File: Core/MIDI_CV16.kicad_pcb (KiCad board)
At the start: 2 copper layers, 59.5 x 99.5 mm, 166 parts, among them J1 USB_C_Receptacle_USB2.0, J2 Conn_01x06_Male, J20 Conn_02x08_Odd_Even, J3 Conn_01x10_Female, J4 Conn_01x10_Female, J5 Conn_01x04, J7 Conn_01x10_Female, J8 Conn_01x10_Female, Q1 BSS84, Q10 BSS84, Q11 2N7002, Q12 2N7002, Q13 BSS84, Q14 2N7002, Q15 BSS84, Q16 BSS84, Q17 2N7002, Q2 BSS84, Q3 2N7002, Q4 BSS84, Q5 BSS84, Q6 2N7002, Q7 BSS84, Q8 2N7002, Q9 BSS84, SW1 SW_Push_DPDT, SW2 SW_SPST, SW3 SW_SPST, U1 RP2040, U10 TL072, U11 TL072, U12 TL072, U13 MCP2517FD-xSL, U14 TLE9250V, U15 MAX5134, U16 CAT25640, U17 IS25LP032D, U2 TMUX4052, U3 MIC5504-3.3YM5, U4 TL072, U5 TL072, U6 TL072, U7 TL072, U8 TMUX4052, U9 TL072, Y1 20MHz, Y2 ECS-120-18-33-JGN-TR3

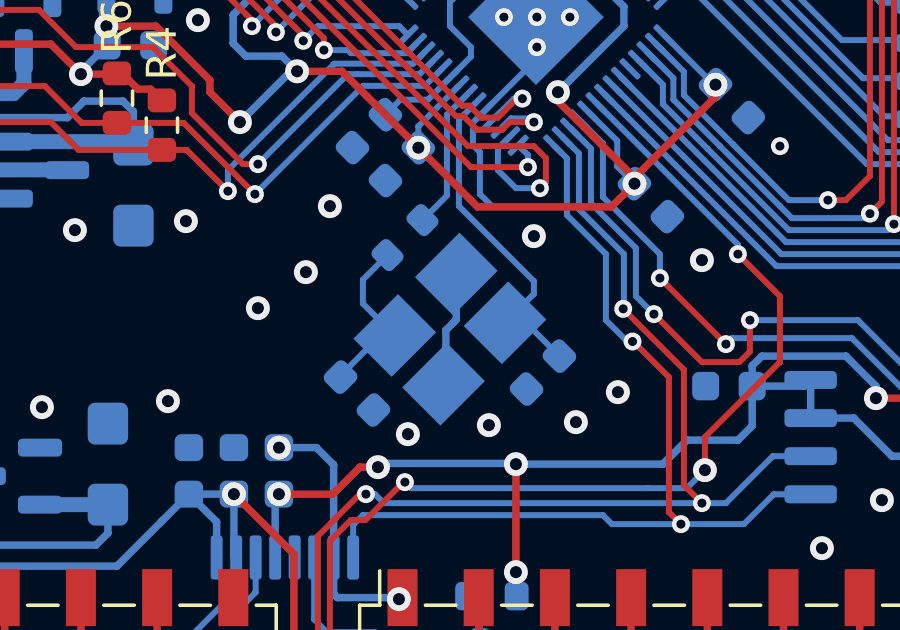
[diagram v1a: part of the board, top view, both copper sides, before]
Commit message: Shrink crystal fp and add silkscreen text
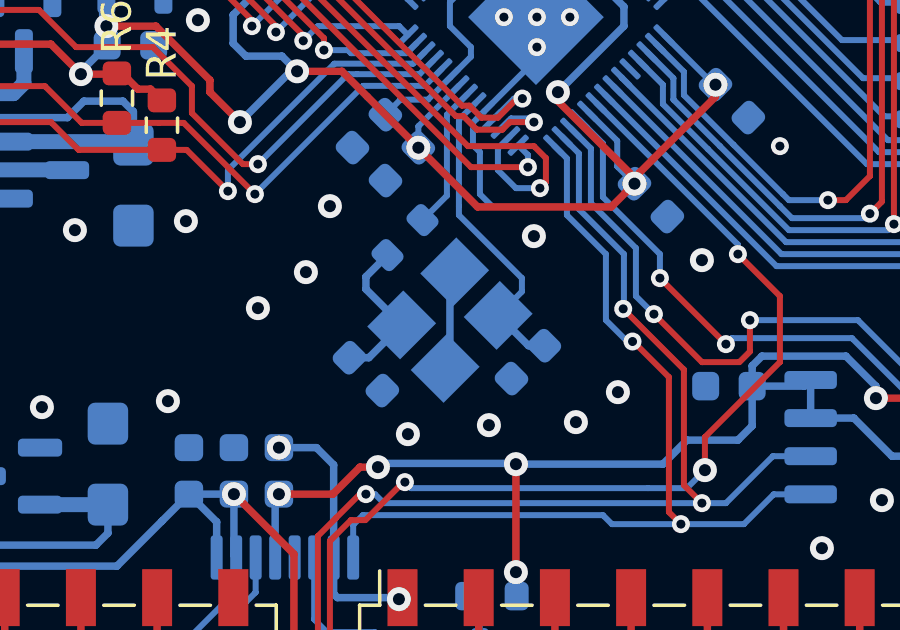
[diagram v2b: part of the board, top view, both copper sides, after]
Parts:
- Y2: footprint Crystal:Crystal_SMD_3225-4Pin_3.2x2.5mm_HandSoldering -> Custom_FP:Crystal_SMD_3225-4Pin_3.2x2.5mm_HandSoldering
- moved C60 0.71 mm to (81.6, 105.4)
- moved C61 0.61 mm to (87.0, 105.0)
- moved Y2 0.30 mm to (84.4, 103.6)
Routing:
- net Net-(U1-XIN): track 11.3 -> 10.5 mm
- net Net-(C60-Pad2): track 5.87 -> 5.31 mm
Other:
- board text added: "-12V"
- board text added: "LED-MATRIX BRIGHTNESS"

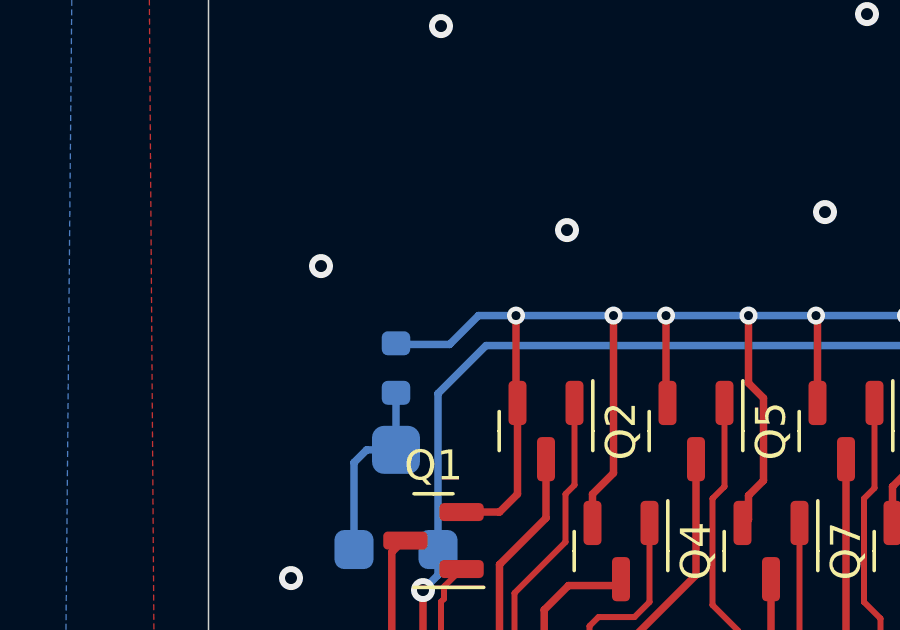
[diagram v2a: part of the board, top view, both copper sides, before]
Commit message: Consolidate resistor values
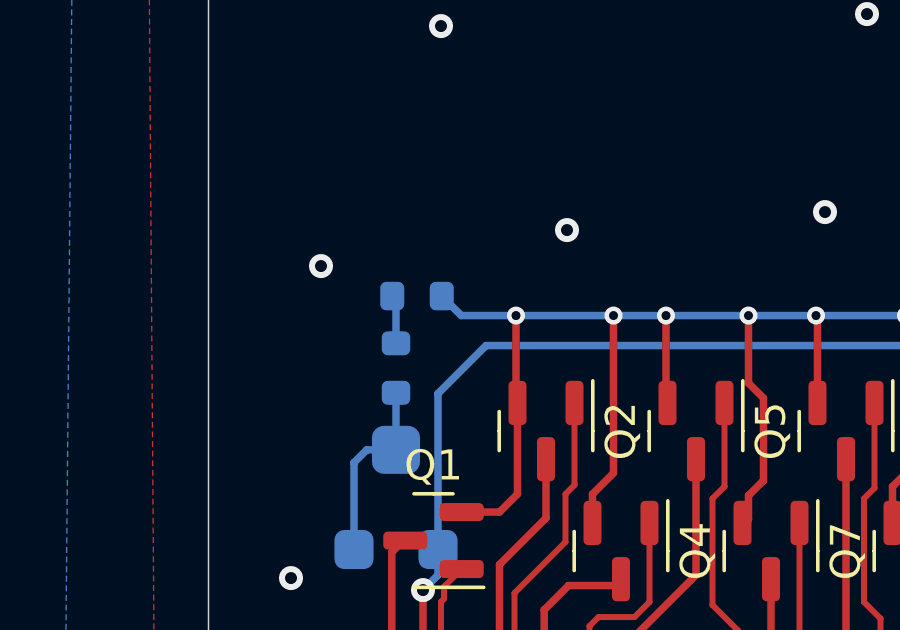
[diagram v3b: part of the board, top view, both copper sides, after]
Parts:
- added R8: 62, Resistor_SMD:R_0603_1608Metric, B.Cu at (57.2, 62.6)
- R63: value 120 -> 62
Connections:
- R63 pad 2: Net-(Q1-S) -> Net-(R63-Pad2)
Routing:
- net Net-(Q1-S): track 58.2 -> 56.5 mm
- net Net-(R63-Pad2): track 0.00 -> 1.63 mm
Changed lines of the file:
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@@
   (net 154 "Net-(J3-Pin_1)")
   (net 155 "Net-(J4-Pin_10)")
+  (net 156 "Net-(R63-Pad2)")
   (footprint "Capacitor_SMD:C_0603_1608Metric" (layer "F.Cu")
     (at 53.5 126.125 90)
@@
         (effects (font (size 1 1) (thickness 0.15)) (justify mirror))
     )
-    (fp_text value "120" (at 0 -1.43 90) (layer "B.Fab")
+    (fp_text value "62" (at 0 -1.43 90) (layer "B.Fab")
         (effects (font (size 1 1) (thickness 0.15)) (justify mirror))
     )
@@
       (net 75 "Net-(R63-Pad1)") (pintype "passive"))
     (pad "2" smd roundrect (at 0.825 0 90) (size 0.8 0.95) (layers "B.Cu" "B.Paste" "B.Mask") (roundrect_rratio 0.25)
-      (net 97 "Net-(Q1-S)") (pintype "passive"))
+      (net 156 "Net-(R63-Pad2)") (pintype "passive"))
     (model "${KICAD6_3DMODEL_DIR}/Resistor_SMD.3dshapes/R_0603_1608Metric.wrl"
       (offset (xyz 0 0 0))
@@
     )
   )
+  (footprint "Resistor_SMD:R_0603_1608Metric" (layer "B.Cu")
+    (at 57.2 62.6)
+    (descr "Resistor SMD 0603 (1608 Metric), square (rectangular) end terminal, IPC_7351 nominal, (Body size source: IPC-SM-782 page 72, https://www.pcb-3d.com/wordpress/wp-content/uploads/ipc-sm-782a_amendment_1_and_2.pdf), generated with kicad-footprint-generator")
+    (tags "resistor")
+    (property "Sheetfile" "HI.kicad_sch")
+    (property "Sheetname" "Human Interface")
+    (property "ki_description" "Resistor")
+    (property "ki_keywords" "R res resistor")
+    (attr smd)
+    (fp_text reference "R8" (at 0 -1.4) (layer "B.SilkS")
+        (effects (font (size 1 1) (thickness 0.15)) (justify mirror))
+    )
+    (fp_text value "62" (at 0 -1.43) (layer "B.Fab")
+        (effects (font (size 1 1) (thickness 0.15)) (justify mirror))
+    )
+    (fp_text user "${REFERENCE}" (at 0 0) (layer "B.Fab")
+        (effects (font (size 0.4 0.4) (thickness 0.06)) (justify mirror))
+    )
+    (fp_line (start -0.237258 -0.5225) (end 0.237258 -0.5225)
+      (stroke (width 0.12) (type solid)) (layer "B.SilkS"))
+    (fp_line (start -0.237258 0.5225) (end 0.237258 0.5225)
+      (stroke (width 0.12) (type solid)) (layer "B.SilkS"))
+    (fp_line (start -1.48 -0.73) (end -1.48 0.73)
+      (stroke (width 0.05) (type solid)) (layer "B.CrtYd"))
+    (fp_line (start -1.48 0.73) (end 1.48 0.73)
+      (stroke (width 0.05) (type solid)) (layer "B.CrtYd"))
+    (fp_line (start 1.48 -0.73) (end -1.48 -0.73)
+      (stroke (width 0.05) (type solid)) (layer "B.CrtYd"))
+    (fp_line (start 1.48 0.73) (end 1.48 -0.73)
+      (stroke (width 0.05) (type solid)) (layer "B.CrtYd"))
+    (fp_line (start -0.8 -0.4125) (end -0.8 0.4125)
+      (stroke (width 0.1) (type solid)) (layer "B.Fab"))
+    (fp_line (start -0.8 0.4125) (end 0.8 0.4125)
+      (stroke (width 0.1) (type solid)) (layer "B.Fab"))
+    (fp_line (start 0.8 -0.4125) (end -0.8 -0.4125)
+      (stroke (width 0.1) (type solid)) (layer "B.Fab"))
+    (fp_line (start 0.8 0.4125) (end 0.8 -0.4125)
+      (stroke (width 0.1) (type solid)) (layer "B.Fab"))
+    (pad "1" smd roundrect (at -0.825 0) (size 0.8 0.95) (layers "B.Cu" "B.Paste" "B.Mask") (roundrect_rratio 0.25)
+      (net 156 "Net-(R63-Pad2)") (pintype "passive"))
+    (pad "2" smd roundrect (at 0.825 0) (size 0.8 0.95) (layers "B.Cu" "B.Paste" "B.Mask") (roundrect_rratio 0.25)
+      (net 97 "Net-(Q1-S)") (pintype "passive"))
+    (model "${KICAD6_3DMODEL_DIR}/Resistor_SMD.3dshapes/R_0603_1608Metric.wrl"
+      (offset (xyz 0 0 0))
+      (scale (xyz 1 1 1))
+      (rotate (xyz 0 0 0))
+    )
+  )
   (footprint "Package_TO_SOT_SMD:SOT-23" (layer "B.Cu")
     (at 70.7 98.6)
@@
   (via (at 70.5 63.25) (size 0.6) (drill 0.3) (layers "F.Cu" "B.Cu") (net 97))
   (via (at 68.25 63.25) (size 0.6) (drill 0.3) (layers "F.Cu" "B.Cu") (net 97))
+  (segment (start 58.675 63.25) (end 58.025 62.6) (width 0.25) (layer "B.Cu") (net 97))
   (segment (start 70.5 63.25) (end 68.25 63.25) (width 0.25) (layer "B.Cu") (net 97))
-  (segment (start 60.5 63.25) (end 59.25 63.25) (width 0.25) (layer "B.Cu") (net 97))
   (segment (start 73.5 63.25) (end 75.5 63.25) (width 0.25) (layer "B.Cu") (net 97))
+  (segment (start 60.5 63.25) (end 58.675 63.25) (width 0.25) (layer "B.Cu") (net 97))
   (segment (start 73.5 63.25) (end 70.5 63.25) (width 0.25) (layer "B.Cu") (net 97))
-  (segment (start 59.25 63.25) (end 58.2875 64.2125) (width 0.25) (layer "B.Cu") (net 97))
   (segment (start 63.75 63.25) (end 60.5 63.25) (width 0.25) (layer "B.Cu") (net 97))
-  (segment (start 58.2875 64.2125) (end 56.5 64.2125) (width 0.25) (layer "B.Cu") (net 97))
   (segment (start 68.25 63.25) (end 65.5 63.25) (width 0.25) (layer "B.Cu") (net 97))
   (segment (start 65.5 63.25) (end 63.75 63.25) (width 0.25) (layer "B.Cu") (net 97))
@@
   (segment (start 53.8 79.6) (end 53.8 85.775) (width 0.25) (layer "B.Cu") (net 155))
   (segment (start 53.8 85.775) (end 54 85.975) (width 0.25) (layer "B.Cu") (net 155))
+  (segment (start 56.5 62.725) (end 56.375 62.6) (width 0.25) (layer "B.Cu") (net 156))
+  (segment (start 56.5 64.175) (end 56.5 62.725) (width 0.25) (layer "B.Cu") (net 156))
   (zone (net 1) (net_name "GND") (layer "F.Cu") (hatch edge 0.508)
     (connect_pads (clearance 0.4))

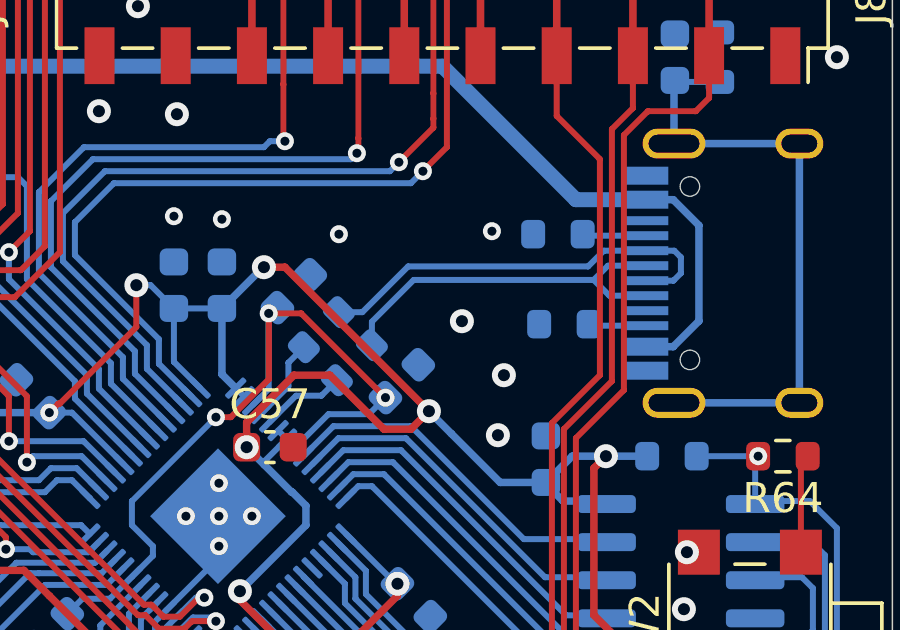
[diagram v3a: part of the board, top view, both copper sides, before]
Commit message: Improve USB impedance and power headroom
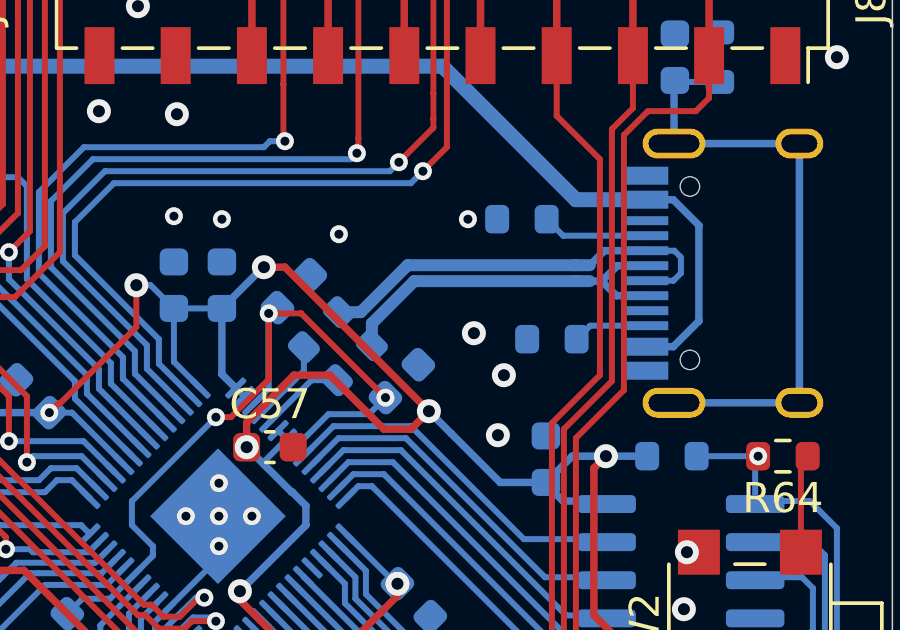
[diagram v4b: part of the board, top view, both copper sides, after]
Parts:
- moved R2 1.30 mm to (97.4, 83.6)
- moved R3 0.64 mm to (98.4, 87.6)
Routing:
- net Net-(J1-CC1): track 1.88 -> 3.56 mm
- net Net-(J1-CC2): track 1.95 -> 2.52 mm
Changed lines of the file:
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@@
   )
   (footprint "Resistor_SMD:R_0603_1608Metric" (layer "B.Cu")
-    (at 98.6 84.1)
+    (at 97.4 83.6)
     (descr "Resistor SMD 0603 (1608 Metric), square (rectangular) end terminal, IPC_7351 nominal, (Body size source: IPC-SM-782 page 72, https://www.pcb-3d.com/wordpress/wp-content/uploads/ipc-sm-782a_amendment_1_and_2.pdf), generated with kicad-footprint-generator")
     (tags "resistor")
@@
   )
   (footprint "Resistor_SMD:R_0603_1608Metric" (layer "B.Cu")
-    (at 98.8 87.1)
+    (at 98.4 87.6)
     (descr "Resistor SMD 0603 (1608 Metric), square (rectangular) end terminal, IPC_7351 nominal, (Body size source: IPC-SM-782 page 72, https://www.pcb-3d.com/wordpress/wp-content/uploads/ipc-sm-782a_amendment_1_and_2.pdf), generated with kicad-footprint-generator")
     (tags "resistor")
@@
   (via (at 78.8 66.6) (size 0.8) (drill 0.4) (layers "F.Cu" "B.Cu") (free) (net 1))
   (via (at 70.8 59.8) (size 0.8) (drill 0.4) (layers "F.Cu" "B.Cu") (free) (net 1))
-  (via (at 96.4 84) (size 0.6) (drill 0.3) (layers "F.Cu" "B.Cu") (free) (net 1))
+  (via (at 95.6 83.6) (size 0.6) (drill 0.3) (layers "F.Cu" "B.Cu") (free) (net 1))
   (via (at 88.4 93.5) (size 0.6) (drill 0.3) (layers "F.Cu" "B.Cu") (net 1))
   (via (at 52.4 92.4) (size 0.8) (drill 0.4) (layers "F.Cu" "B.Cu") (free) (net 1))
@@
   (via (at 91.3 84.1) (size 0.6) (drill 0.3) (layers "F.Cu" "B.Cu") (free) (net 1))
   (via (at 94.2 114.5) (size 0.8) (drill 0.4) (layers "F.Cu" "B.Cu") (free) (net 1))
-  (via (at 95.4 87) (size 0.8) (drill 0.4) (layers "F.Cu" "B.Cu") (free) (net 1))
+  (via (at 95.8 87.4) (size 0.8) (drill 0.4) (layers "F.Cu" "B.Cu") (free) (net 1))
   (via (at 57.2 101.1) (size 0.8) (drill 0.4) (layers "F.Cu" "B.Cu") (net 1))
   (via (at 83 107.4) (size 0.8) (drill 0.4) (layers "F.Cu" "B.Cu") (free) (net 1))
@@
   (segment (start 87.2 90.2) (end 84.4 93) (width 0.2) (layer "B.Cu") (net 4))
   (segment (start 84.4 93) (end 84.4 93.8) (width 0.2) (layer "B.Cu") (net 4))
+  (segment (start 88.95979 89.263254) (end 88.95979 86.74021) (width 0.2) (layer "B.Cu") (net 4))
   (segment (start 84.413685 95.506415) (end 83.668108 96.251992) (width 0.2) (layer "B.Cu") (net 4))
   (segment (start 89.84073 91.210742) (end 90.951473 90.1) (width 0.2) (layer "B.Cu") (net 4))
@@
   (segment (start 83.668108 96.251992) (end 82.748008 96.251992) (width 0.2) (layer "B.Cu") (net 4))
   (segment (start 85.1 94.5) (end 85.1 94.8201) (width 0.2) (layer "B.Cu") (net 4))
+  (segment (start 88.426516 89.796528) (end 88.95979 89.263254) (width 0.2) (layer "B.Cu") (net 4))
   (segment (start 82.748008 96.251992) (end 82.248008 96.751992) (width 0.2) (layer "B.Cu") (net 4))
-  (segment (start 88.95979 86.74021) (end 88.95979 89.263254) (width 0.2) (layer "B.Cu") (net 4))
-  (segment (start 88.95979 89.263254) (end 88.426516 89.796528) (width 0.2) (layer "B.Cu") (net 4))
   (segment (start 56.235 133.975) (end 56.235 136.0775) (width 0.25) (layer "F.Cu") (net 5))
   (segment (start 56.235 136.0775) (end 56.2 136.1125) (width 0.25) (layer "F.Cu") (net 5))
@@
   (segment (start 84.7 99.8) (end 84.7 100.1) (width 0.2) (layer "B.Cu") (net 26))
   (segment (start 85.262214 96.354944) (end 84.7 96.917158) (width 0.2) (layer "B.Cu") (net 26))
-  (segment (start 101.555 84.15) (end 99.675 84.15) (width 0.2) (layer "B.Cu") (net 27))
+  (segment (start 98.775 84.15) (end 98.225 83.6) (width 0.2) (layer "B.Cu") (net 27))
+  (segment (start 101.555 84.15) (end 98.775 84.15) (width 0.2) (layer "B.Cu") (net 27))
   (segment (start 101.555 87.15) (end 99.675 87.15) (width 0.2) (layer "B.Cu") (net 29))
-  (segment (start 99.675 87.15) (end 99.625 87.1) (width 0.2) (layer "B.Cu") (net 29))
+  (segment (start 99.675 87.15) (end 99.225 87.6) (width 0.2) (layer "B.Cu") (net 29))
   (segment (start 53.695 133.975) (end 53.695 135.5675) (width 0.25) (layer "F.Cu") (net 32))
   (segment (start 51.6 123.3) (end 56.86 118.04) (width 0.25) (layer "F.Cu") (net 32))
@@
   (segment (start 69.25 92.7625) (end 69.25 91.1) (width 0.5) (layer "B.Cu") (net 35))
   (segment (start 99.2 82.95) (end 101.555 82.95) (width 0.5) (layer "B.Cu") (net 35))
-  (segment (start 93.793199 85.625) (end 92.4 87.018199) (width 0.2) (layer "B.Cu") (net 36))
-  (segment (start 100.3182 86.15) (end 99.7932 85.625) (width 0.2) (layer "B.Cu") (net 36))
-  (segment (start 93.793199 85.625) (end 99.7932 85.625) (width 0.2) (layer "B.Cu") (net 36))
-  (segment (start 101.555 85.15) (end 100.2682 85.15) (width 0.2) (layer "B.Cu") (net 36))
-  (segment (start 101.555 86.15) (end 100.3182 86.15) (width 0.2) (layer "B.Cu") (net 36))
-  (segment (start 100.2682 85.15) (end 99.7932 85.625) (width 0.2) (layer "B.Cu") (net 36))
-  (segment (start 92.4 87.018199) (end 92.4 87.8) (width 0.2) (layer "B.Cu") (net 36))
+  (segment (start 92.4 87.074767) (end 93.809767 85.665) (width 0.4) (layer "B.Cu") (net 36))
+  (segment (start 100.55 86.15) (end 101.555 86.15) (width 0.25) (layer "B.Cu") (net 36))
+  (segment (start 101.555 85.15) (end 100.58 85.15) (width 0.25) (layer "B.Cu") (net 36))
+  (segment (start 100.065 85.665) (end 100.55 86.15) (width 0.25) (layer "B.Cu") (net 36))
+  (segment (start 100.58 85.15) (end 100.065 85.665) (width 0.25) (layer "B.Cu") (net 36))
+  (segment (start 100.065 85.665) (end 99.665 85.665) (width 0.25) (layer "B.Cu") (net 36))
+  (segment (start 92.4 87.8) (end 92.4 87.074767) (width 0.4) (layer "B.Cu") (net 36))
+  (segment (start 99.2 85.665) (end 99.665 85.665) (width 0.4) (layer "B.Cu") (net 36))
+  (segment (start 93.809767 85.665) (end 99.2 85.665) (width 0.4) (layer "B.Cu") (net 36))
+  (segment (start 101.555 84.65) (end 100.15 84.65) (width 0.25) (layer "B.Cu") (net 37))
   (segment (start 101.555 85.65) (end 102.45 85.65) (width 0.2) (layer "B.Cu") (net 37))
-  (segment (start 93.606801 85.175) (end 99.6068 85.175) (width 0.2) (layer "B.Cu") (net 37))
-  (segment (start 101.555 84.65) (end 100.1318 84.65) (width 0.2) (layer "B.Cu") (net 37))
+  (segment (start 100.15 84.65) (end 99.665 85.135) (width 0.25) (layer "B.Cu") (net 37))
+  (segment (start 91.3 86.7) (end 92.025233 86.7) (width 0.4) (layer "B.Cu") (net 37))
   (segment (start 102.48 84.65) (end 101.555 84.65) (width 0.2) (layer "B.Cu") (net 37))
-  (segment (start 100.1318 84.65) (end 99.6068 85.175) (width 0.2) (layer "B.Cu") (net 37))
+  (segment (start 92.025233 86.7) (end 93.590233 85.135) (width 0.4) (layer "B.Cu") (net 37))
   (segment (start 102.7 84.87) (end 102.48 84.65) (width 0.2) (layer "B.Cu") (net 37))
+  (segment (start 99.2 85.135) (end 99.665 85.135) (width 0.4) (layer "B.Cu") (net 37))
   (segment (start 102.7 85.4) (end 102.7 84.87) (width 0.2) (layer "B.Cu") (net 37))
-  (segment (start 92.081801 86.7) (end 91.3 86.7) (width 0.2) (layer "B.Cu") (net 37))
-  (segment (start 93.606801 85.175) (end 92.081801 86.7) (width 0.2) (layer "B.Cu") (net 37))
+  (segment (start 93.590233 85.135) (end 99.2 85.135) (width 0.4) (layer "B.Cu") (net 37))
   (segment (start 102.45 85.65) (end 102.7 85.4) (width 0.2) (layer "B.Cu") (net 37))
   (segment (start 71.94 94.5) (end 70.7 93.26) (width 0.2) (layer "F.Cu") (net 38))
@@
   (segment (start 105.335 127.09) (end 105.5 126.925) (width 0.25) (layer "F.Cu") (net 114))
   (segment (start 104 125.275) (end 104 125.425) (width 0.25) (layer "F.Cu") (net 114))
-  (segment (start 89.871053 89.483363) (end 88.992202 90.362214) (width 0.2) (layer "B.Cu") (net 115))
-  (segment (start 90.716637 89.483363) (end 89.871053 89.483363) (width 0.2) (layer "B.Cu") (net 115))
-  (segment (start 91.233274 88.966726) (end 90.716637 89.483363) (width 0.2) (layer "B.Cu") (net 115))
-  (segment (start 89.616637 89.172093) (end 88.709359 90.079371) (width 0.2) (layer "B.Cu") (net 116))
-  (segment (start 90.133274 87.866726) (end 89.616637 88.383363) (width 0.2) (layer "B.Cu") (net 116))
-  (segment (start 89.616637 88.383363) (end 89.616637 89.172093) (width 0.2) (layer "B.Cu") (net 116))
+  (segment (start 88.992202 90.362214) (end 90.387692 88.966726) (width 0.2) (layer "B.Cu") (net 115))
+  (segment (start 90.387692 88.966726) (end 91.233274 88.966726) (width 0.2) (layer "B.Cu") (net 115))
+  (segment (start 90.133274 88.655456) (end 90.133274 87.866726) (width 0.2) (layer "B.Cu") (net 116))
+  (segment (start 88.709359 90.079371) (end 90.133274 88.655456) (width 0.2) (layer "B.Cu") (net 116))
   (via (at 105.275 91.5) (size 0.6) (drill 0.3) (layers "F.Cu" "B.Cu") (net 117))
   (segment (start 105.175 92.995) (end 105.175 91.6) (width 0.2) (layer "B.Cu") (net 117))
